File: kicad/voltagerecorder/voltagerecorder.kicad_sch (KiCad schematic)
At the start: 35 parts, among them J1 Conn_02x10_Odd_Even, J2 Phoenix Stecker, J3 Conn_01x08, J8 Conn_01x02, U1 Opamp_Quad, U5 ADS8638, U6 ESP32-S3-WROOM-2, Y1 32.768kHz

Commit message: sd card hinzugefügt
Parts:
- removed Y1: 32.768kHz, Crystal:Crystal_SMD_SeikoEpson_MC306-4Pin_8.0x3.2mm_HandSoldering, symbol Device:Crystal
- added J9: Micro_SD_Card, Connector_Card:microSD_HC_Hirose_DM3BT-DSF-PEJS, symbol Connector:Micro_SD_Card
- added Y1: Crystal_GND23, Crystal:Crystal_SMD_SeikoEpson_MC306-4Pin_8.0x3.2mm_HandSoldering, symbol Device:Crystal_GND23
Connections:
- net at C24.1, U6.8 (GPIO15/U0RTS/ADC2_CH4/XTAL_32K_P): now also Y1.4
- net at C29.1, U6.9 (GPIO16/U0CTS/ADC2_CH5/XTAL_32K_NH5): now also Y1.1
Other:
- note added: "2 pin Pheonix Trigger in and out"
- note added: "3 pin 5V, 24V, GND"
- note added: "AC/DC 230V 5V ??"
- note added: "DC/DC 24V 5V ??"
- note added: "SD Karte"
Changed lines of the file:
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@@
   (junction (at 160.02 81.28) (diameter 0) (color 0 0 0 0)
   )
-  (junction (at 110.49 194.31) (diameter 0) (color 0 0 0 0)
-  )
   (junction (at 171.45 73.66) (diameter 0) (color 0 0 0 0)
   )
@@
   (junction (at 110.49 142.24) (diameter 0) (color 0 0 0 0)
   )
-  (junction (at 110.49 201.93) (diameter 0) (color 0 0 0 0)
+  (junction (at 111.76 194.31) (diameter 0) (color 0 0 0 0)
   )
   (junction (at 270.51 58.42) (diameter 0) (color 0 0 0 0)
@@
   (junction (at 160.02 99.06) (diameter 0) (color 0 0 0 0)
   )
+  (junction (at 111.76 201.93) (diameter 0) (color 0 0 0 0)
+  )
   (junction (at 171.45 81.28) (diameter 0) (color 0 0 0 0)
   )
@@
     (stroke (width 0) (type default) (color 0 0 0 0))
   )
-  (wire (pts (xy 125.73 194.31) (xy 110.49 194.31))
+  (wire (pts (xy 106.68 194.31) (xy 111.76 194.31))
     (stroke (width 0) (type default) (color 0 0 0 0))
   )
@@
     (stroke (width 0) (type default) (color 0 0 0 0))
   )
-  (wire (pts (xy 106.68 194.31) (xy 110.49 194.31))
-    (stroke (width 0) (type default) (color 0 0 0 0))
-  )
   (wire (pts (xy 297.18 66.04) (xy 297.18 68.58))
     (stroke (width 0) (type default) (color 0 0 0 0))
@@
     (stroke (width 0) (type default) (color 0 0 0 0))
   )
+  (wire (pts (xy 111.76 194.31) (xy 125.73 194.31))
+    (stroke (width 0) (type default) (color 0 0 0 0))
+  )
   (wire (pts (xy 297.18 48.26) (xy 297.18 50.8))
     (stroke (width 0) (type default) (color 0 0 0 0))
@@
     (stroke (width 0) (type default) (color 0 0 0 0))
   )
+  (wire (pts (xy 111.76 201.93) (xy 125.73 201.93))
+    (stroke (width 0) (type default) (color 0 0 0 0))
+  )
   (wire (pts (xy 171.45 86.36) (xy 179.07 86.36))
     (stroke (width 0) (type default) (color 0 0 0 0))
@@
     (stroke (width 0) (type default) (color 0 0 0 0))
   )
-  (wire (pts (xy 106.68 201.93) (xy 110.49 201.93))
-    (stroke (width 0) (type default) (color 0 0 0 0))
-  )
   (wire (pts (xy 130.81 106.68) (xy 134.62 106.68))
     (stroke (width 0) (type default) (color 0 0 0 0))
@@
     (stroke (width 0) (type default) (color 0 0 0 0))
   )
-  (wire (pts (xy 125.73 201.93) (xy 110.49 201.93))
+  (wire (pts (xy 106.68 201.93) (xy 111.76 201.93))
     (stroke (width 0) (type default) (color 0 0 0 0))
   )
@@
   (wire (pts (xy 74.93 71.12) (xy 74.93 64.77))
     (stroke (width 0) (type default) (color 0 0 0 0))
+  )
+  (text "AC/DC 230V 5V ??" (at 312.42 194.31 0)
+    (effects (font (size 2.54 2.54)) (justify left bottom))
   )
   (text "L1" (at 30.48 72.0725 0)
@@
     (effects (font (size 2.54 2.54)) (justify left bottom))
   )
+  (text "2 pin Pheonix Trigger in and out" (at 312.42 175.26 0)
+    (effects (font (size 2.54 2.54)) (justify left bottom))
+  )
   (text "AL_PD:\nlow active\ninternal pull up" (at 201.93 72.39 0)
     (effects (font (size 1.27 1.27)) (justify left bottom))
@@
   (text "L3" (at 30.48 77.1525 0)
     (effects (font (size 1.27 1.27)) (justify left bottom))
+  )
+  (text "DC/DC 24V 5V ??" (at 312.42 187.96 0)
+    (effects (font (size 2.54 2.54)) (justify left bottom))
+  )
+  (text "SD Karte" (at 312.42 168.91 0)
+    (effects (font (size 2.54 2.54)) (justify left bottom))
   )
   (text "C0G" (at 114.3 93.9801 0)
@@
     (at 129.54 115.57 0)
     (effects (font (size 1.27 1.27)) (justify left bottom))
+  )
+  (text "3 pin 5V, 24V, GND" (at 312.42 181.61 0)
+    (effects (font (size 2.54 2.54)) (justify left bottom))
   )
   (label "IN5_EXT" (at 87.63 41.91 270)
@@
     (pin "4")
   )
+  (symbol (lib_id "Connector:Micro_SD_Card") (at 325.12 224.79 0) (unit 1)
+    (in_bom yes) (on_board yes) (fields_autoplaced)
+    (property "Reference" "J9" (id 0) (at 325.755 205.74 0))
+    (property "Value" "Micro_SD_Card" (id 1) (at 325.755 208.28 0))
+    (property "Footprint" "Connector_Card:microSD_HC_Hirose_DM3BT-DSF-PEJS" (id 2) (at 354.33 217.17 0)
+      (effects (font (size 1.27 1.27)) hide)
+    )
+    (property "Datasheet" "http://katalog.we-online.de/em/datasheet/693072010801.pdf" (id 3) (at 325.12 224.79 0)
+      (effects (font (size 1.27 1.27)) hide)
+    )
+    (pin "1")
+    (pin "2")
+    (pin "3")
+    (pin "4")
+    (pin "5")
+    (pin "6")
+    (pin "7")
+    (pin "8")
+    (pin "9")
+  )
+  (symbol (lib_id "Device:Crystal_GND23") (at 111.76 198.12 90) (unit 1)
+    (in_bom yes) (on_board yes) (fields_autoplaced)
+    (property "Reference" "Y1" (id 0) (at 124.46 193.421 90))
+    (property "Value" "Crystal_GND23" (id 1) (at 124.46 195.961 90))
+    (property "Footprint" "Crystal:Crystal_SMD_SeikoEpson_MC306-4Pin_8.0x3.2mm_HandSoldering" (id 2) (at 111.76 198.12 0)
+      (effects (font (size 1.27 1.27)) hide)
+    )
+    (property "Datasheet" "~" (id 3) (at 111.76 198.12 0)
+      (effects (font (size 1.27 1.27)) hide)
+    )
+    (pin "1")
+    (pin "2")
+    (pin "3")
+    (pin "4")
+  )
   (symbol (lib_id "Device:C") (at 96.52 73.66 0) (unit 1)
     (in_bom yes) (on_board yes)
@@
     )
     (property "Datasheet" "~" (id 3) (at 171.45 90.17 0)
-      (effects (font (size 1.27 1.27)) hide)
-    )
-    (pin "1")
-    (pin "2")
-  )
-  (symbol (lib_id "Device:Crystal") (at 110.49 198.12 270) (unit 1)
-    (in_bom yes) (on_board yes) (fields_autoplaced)
-    (property "Reference" "Y1" (id 0) (at 114.3 196.8499 90)
-      (effects (font (size 1.27 1.27)) (justify left))
-    )
-    (property "Value" "32.768kHz" (id 1) (at 114.3 199.3899 90)
-      (effects (font (size 1.27 1.27)) (justify left))
-    )
-    (property "Footprint" "Crystal:Crystal_SMD_SeikoEpson_MC306-4Pin_8.0x3.2mm_HandSoldering" (id 2) (at 110.49 198.12 0)
-      (effects (font (size 1.27 1.27)) hide)
-    )
-    (property "Datasheet" "~" (id 3) (at 110.49 198.12 0)
       (effects (font (size 1.27 1.27)) hide)
     )
@@
       (reference "J8") (unit 1) (value "Conn_01x02") (footprint "Connector_PinHeader_2.54mm:PinHeader_1x02_P2.54mm_Vertical")
     )
+    (path "/9c543bc0-4531-49c8-a9a3-3bab9988c097"
+      (reference "J9") (unit 1) (value "Micro_SD_Card") (footprint "Connector_Card:microSD_HC_Hirose_DM3BT-DSF-PEJS")
+    )
     (path "/9767ed14-54f6-47aa-91eb-a27d04c45e2a"
       (reference "JP1") (unit 1) (value "SolderJumper_3_Open") (footprint "Jumper:SolderJumper-3_P1.3mm_Open_RoundedPad1.0x1.5mm")
@@
       (reference "U7") (unit 1) (value "L78L12ACUTR") (footprint "Package_TO_SOT_SMD:SOT-89-3_Handsoldering")
     )
-    (path "/bd8055c5-bb05-44e7-a2eb-64493be9f622"
-      (reference "Y1") (unit 1) (value "32.768kHz") (footprint "Crystal:Crystal_SMD_SeikoEpson_MC306-4Pin_8.0x3.2mm_HandSoldering")
-    )
-  )
+    (path "/a087b7ce-d9b0-4ba0-8285-fc2f36d419e2"
+      (reference "Y1") (unit 1) (value "Crystal_GND23") (footprint "Crystal:Crystal_SMD_SeikoEpson_MC306-4Pin_8.0x3.2mm_HandSoldering")
+    )
+  )

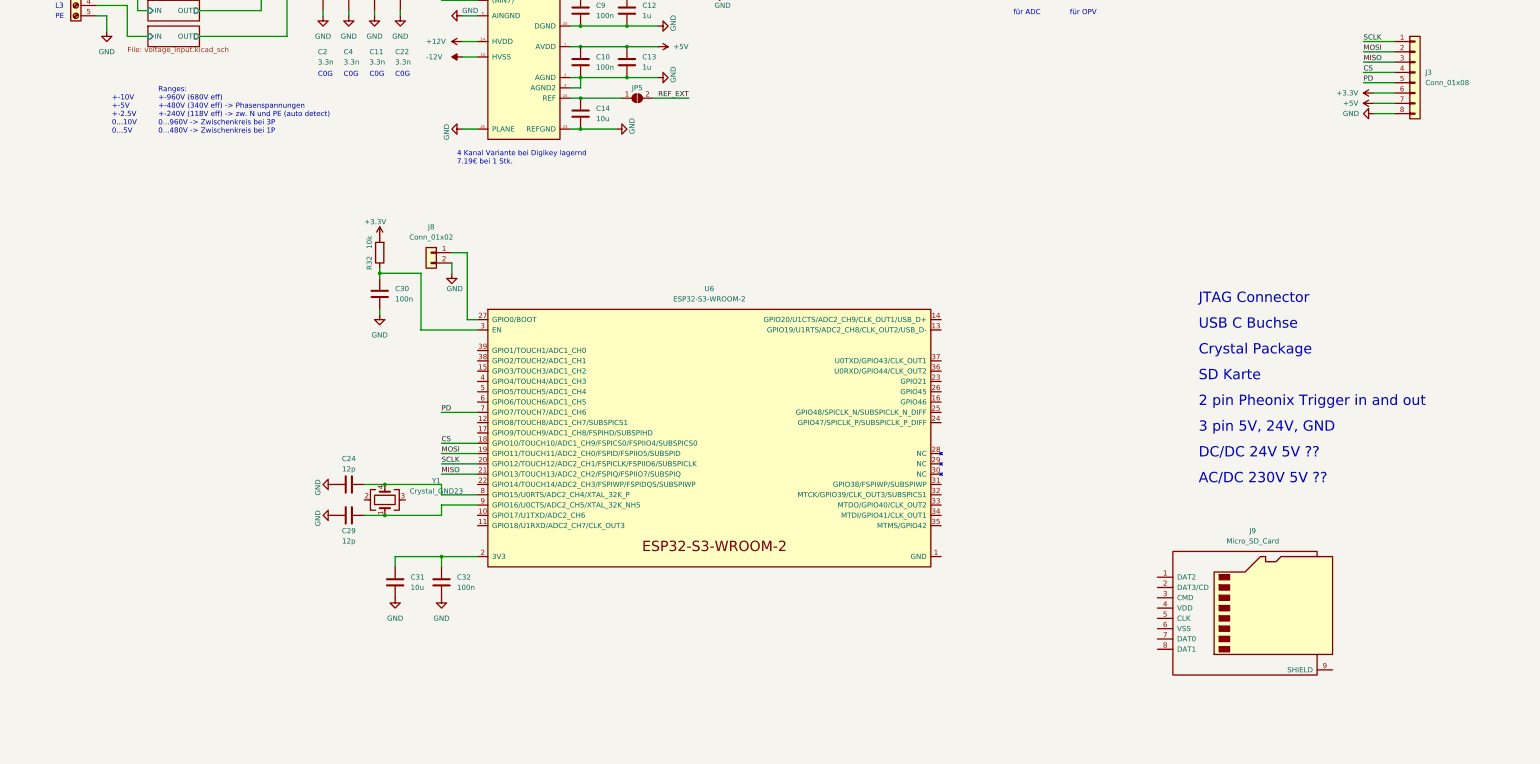
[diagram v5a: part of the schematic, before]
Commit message: SD und USB-C added.
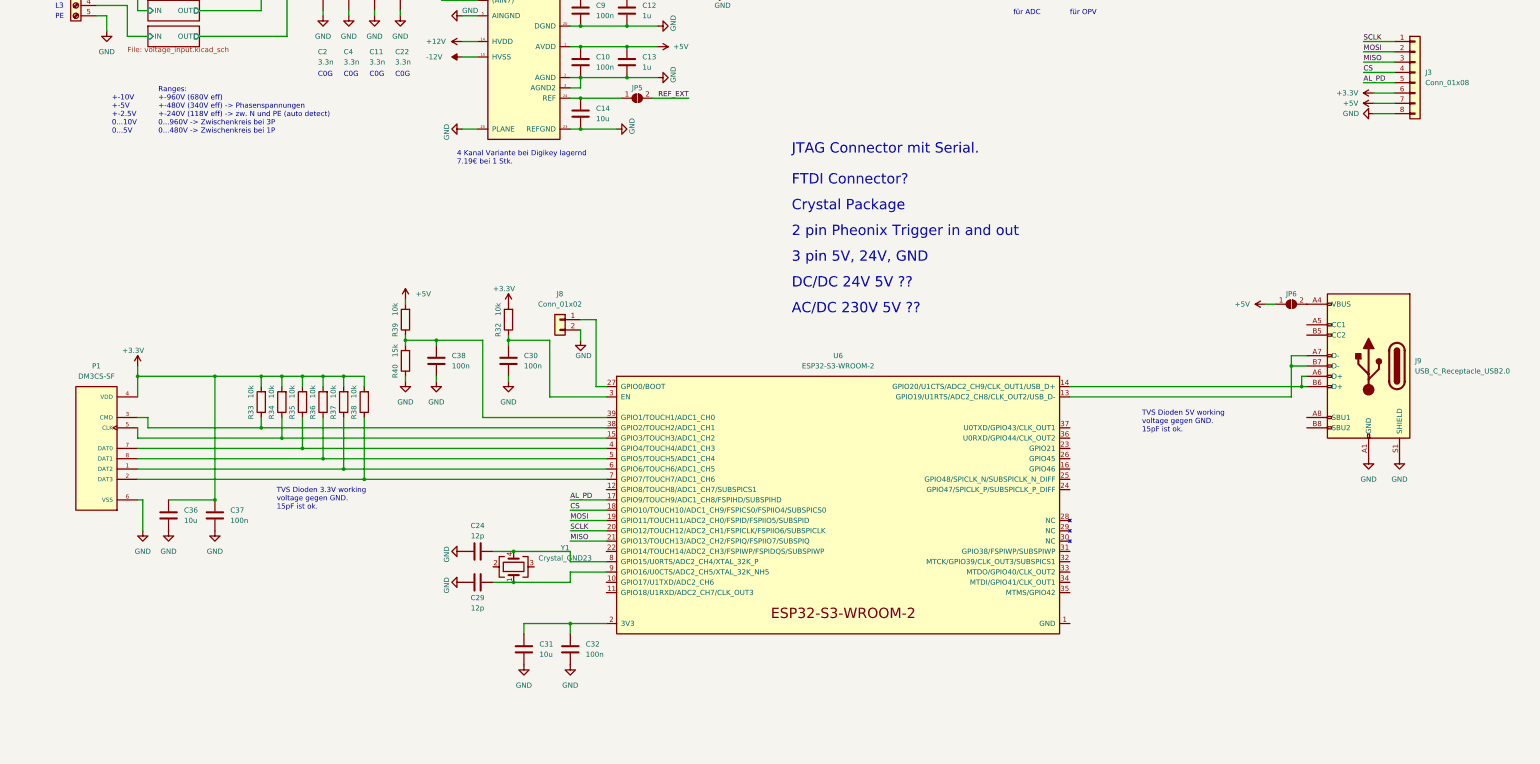
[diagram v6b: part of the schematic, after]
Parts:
- removed J9: Micro_SD_Card, Connector_Card:microSD_HC_Hirose_DM3BT-DSF-PEJS, symbol Connector:Micro_SD_Card
- added C36: 10u, Capacitor_SMD:C_0805_2012Metric_Pad1.18x1.45mm_HandSolder, symbol Device:C
- added C37, C38: 100n, Capacitor_SMD:C_0603_1608Metric_Pad1.08x0.95mm_HandSolder, symbol Device:C
- added J9: USB_C_Receptacle_USB2.0, Connector_USB:USB_C_Receptacle_GCT_USB4085, symbol Connector:USB_C_Receptacle_USB2.0
- added JP6: SolderJumper_2_Open, Jumper:SolderJumper-2_P1.3mm_Open_RoundedPad1.0x1.5mm, symbol Jumper:SolderJumper_2_Open
- added P1: DM3CS-SF, Hirose:HRS_DM3CS-SF, symbol Hirose:DM3CS-SF
- added R33, R34, R35, R36, R37, R38, R39: 10k, Resistor_SMD:R_0603_1608Metric_Pad0.98x0.95mm_HandSolder, symbol Device:R
- added R40: 15k, Resistor_SMD:R_0603_1608Metric_Pad0.98x0.95mm_HandSolder, symbol Device:R
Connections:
- net +3.3V: now also C36.1, C37.1, P1.4 (VDD), R33.2, R34.2, R35.2, R36.2, R37.2, R38.2
- net +5V: now also JP6.1 (A), R39.2
- net AL_PD: now also J3.5 (Pin_5), U6.17 (GPIO9/TOUCH9/ADC1_CH8/FSPIHD/SUBSPIHD)
- net GND: now also C36.2, C37.2, C38.2, J9.A1 (GND), J9.A12 (GND), J9.B1 (GND), J9.B12 (GND), J9.S1 (SHIELD), P1.6 (VSS), R40.1
- net at U6.13 (GPIO19/U1RTS/ADC2_CH8/CLK_OUT2/USB_D-): now also J9.A7 (D-), J9.B7 (D-)
- net at U6.14 (GPIO20/U1CTS/ADC2_CH9/CLK_OUT1/USB_D+): now also J9.A6 (D+), J9.B6 (D+)
- net at U6.15 (GPIO3/TOUCH3/ADC1_CH2): now also P1.5 (CLK), R34.1
- net at U6.38 (GPIO2/TOUCH2/ADC1_CH1): now also P1.3 (CMD), R33.1
- net at U6.39 (GPIO1/TOUCH1/ADC1_CH0): now also C38.1, R39.1, R40.2
- net at U6.4 (GPIO4/TOUCH4/ADC1_CH3): now also P1.7 (DAT0), R35.1
- net at U6.5 (GPIO5/TOUCH5/ADC1_CH4): now also P1.8 (DAT1), R36.1
- net at U6.6 (GPIO6/TOUCH6/ADC1_CH5): now also P1.1 (DAT2), R37.1
- net PD: no longer names the net of U6.7 (GPIO7/TOUCH7/ADC1_CH6)
- net PD: now also P1.2 (DAT3), R38.1; no longer J3.5 (Pin_5)
- new net: J9.A4 (VBUS), J9.A9 (VBUS), J9.B4 (VBUS), J9.B9 (VBUS), JP6.2 (B)
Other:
- note added: "FTDI Connector?"
- note added: "JTAG Connector mit Serial."
- note added: "TVS Dioden 3.3V working voltage gegen GND. 15pF ist ok."
- note added: "TVS Dioden 5V working voltage gegen GND. 15pF ist ok."
- note removed: "JTAG Connector"
- note removed: "SD Karte"
- note removed: "USB C Buchse"
- moved on the sheet: C24, C29, C30, C31, C32, J8, R32, U6, Y1

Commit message: a
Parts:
- removed C24, C29: 12p, Capacitor_SMD:C_0603_1608Metric_Pad1.08x0.95mm_HandSolder, symbol Device:C
- removed C30, C32: 100n, Capacitor_SMD:C_0603_1608Metric_Pad1.08x0.95mm_HandSolder, symbol Device:C
- removed C31: 10u, Capacitor_SMD:C_0805_2012Metric_Pad1.18x1.45mm_HandSolder, symbol Device:C
- removed J2: Phoenix Stecker, Connector_Phoenix_MC_HighVoltage:PhoenixContact_MC_1,5_5-G-5.08_1x05_P5.08mm_Horizontal, symbol Connector:Screw_Terminal_01x05
- removed J8: Conn_01x02, Connector_PinHeader_2.54mm:PinHeader_1x02_P2.54mm_Vertical, symbol Connector_Generic:Conn_01x02
- removed J9: USB_C_Receptacle_USB2.0, Connector_USB:USB_C_Receptacle_GCT_USB4085, symbol Connector:USB_C_Receptacle_USB2.0
- removed JP6: SolderJumper_2_Open, Jumper:SolderJumper-2_P1.3mm_Open_RoundedPad1.0x1.5mm, symbol Jumper:SolderJumper_2_Open
- removed R32: 10k, Resistor_SMD:R_0603_1608Metric_Pad0.98x0.95mm_HandSolder, symbol Device:R
- removed U6: ESP32-S3-WROOM-2, Espressif:ESP32-S3-WROOM-2, symbol espressif:ESP32-S3-WROOM-2
- removed Y1: Crystal_GND23, Crystal:Crystal_SMD_SeikoEpson_MC306-4Pin_8.0x3.2mm_HandSoldering, symbol Device:Crystal_GND23
- added C? (x6): 100nF, Capacitor_SMD:C_0603_1608Metric, symbol Device:C
- added C? (x2): 10nF, Capacitor_SMD:C_0603_1608Metric, symbol Device:C
- added C? (x2): 1uF, Capacitor_SMD:C_0603_1608Metric, symbol Device:C
- added C?: 1u, Capacitor_SMD:C_0603_1608Metric_Pad1.08x0.95mm_HandSolder, symbol Device:C
- added C? (x2): 22pF, Capacitor_SMD:C_0603_1608Metric, symbol Device:C
- added C?: 4.7uF, Capacitor_SMD:C_0603_1608Metric, symbol Device:C
- added D?: D_Schottky, Diode_SMD:D_0603_1608Metric_Pad1.05x0.95mm_HandSolder, symbol Device:D_Schottky
- added D?: RED, Diode_SMD:D_0603_1608Metric, symbol Device:LED_Filled
- added D?: GREEN, Diode_SMD:D_0603_1608Metric, symbol Device:LED_Filled
- added D?: YELLOW, Diode_SMD:D_0603_1608Metric, symbol Device:LED_Filled
- added FB?: 220R / 100MHz, Inductor_SMD:L_0603_1608Metric_Pad1.05x0.95mm_HandSolder, symbol Device:FerriteBead
- added H? (x6): MountingHole_Pad, MountingHole:MountingHole_3.2mm_M3_DIN965_Pad, symbol Mechanical:MountingHole_Pad
- added J?: Conn_01x05, Connector_Phoenix_MSTB:PhoenixContact_MSTBA_2,5_5-G-5,08_1x05_P5.08mm_Horizontal, symbol Connector_Generic:Conn_01x05
- added J? (x2): Conn_01x02, Connector_PinHeader_2.54mm:PinHeader_1x02_P2.54mm_Vertical, symbol Connector_Generic:Conn_01x02
- added J? (x2): USB_C_Receptacle_USB2.0, Connector_USB:USB_C_Receptacle_XKB_U262-16XN-4BVC11, symbol Connector:USB_C_Receptacle_USB2.0
- added J?: Conn_01x08, Connector_PinHeader_2.54mm:PinHeader_1x08_P2.54mm_Horizontal, symbol Connector_Generic:Conn_01x08
- added R? (x2): 1M, Resistor_SMD:R_0603_1608Metric, symbol Device:R
- added R? (x3): 1k, Resistor_SMD:R_0603_1608Metric, symbol Device:R
- added R?: 10k, Resistor_SMD:R_0603_1608Metric, symbol Device:R
- added R?: 100k, Resistor_SMD:R_0603_1608Metric, symbol Device:R
- added R? (x2): 3k3, Resistor_SMD:R_0603_1608Metric_Pad0.98x0.95mm_HandSolder, symbol Device:R
- added U8: ESP32-C3-WROOM-02, Espressif:ESP32-C3-WROOM-02, symbol espressif:ESP32-C3-WROOM-02
- added U?: ESP-PSRAM32, Package_SO:SOIC-8_3.9x4.9mm_P1.27mm, symbol Memory_RAM:ESP-PSRAM32
- added U? (x2): STM32G473CBT6, Package_QFP:LQFP-48_7x7mm_P0.5mm, symbol wittmann:STM32G473CBT6
- added Y?: 24MHz, Crystal:Crystal_SMD_3225-4Pin_3.2x2.5mm, symbol Device:Crystal_GND24
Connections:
- net +3.3V: now also C?.1, D?.2 (A), D?.2 (A), D?.2 (A), R?.2, R?.2, U?.8 (VCC)
- net +5V: now also D?.2 (A)
- net GND: now also C?.2, C?.2, C?.2, C?.2, C?.2, C?.2, C?.2, C?.2, C?.2, C?.2, C?.2, C?.2, C?.2, C?.2, J?.1 (Pin_1), J?.2 (Pin_2), J?.5 (Pin_5), J?.7 (Pin_7), J?.A1 (GND), J?.A1 (GND), J?.A12 (GND), J?.A12 (GND), J?.B1 (GND), J?.B1 (GND), J?.B12 (GND), J?.B12 (GND), R?.1, R?.2, R?.2, U8.19 (GND), U8.9 (GND), U?.19 (VSSA), U?.23 (VSS), U?.35 (VSS), U?.4 (VSS), U?.47 (VSS), Y?.2, Y?.4
- net voltage_input/IN: now also J?.2 (Pin_2)
- net voltage_input1/IN: now also J?.3 (Pin_3)
- net voltage_input2/IN: now also J?.4 (Pin_4)
- net voltage_input3/IN: now also J?.1 (Pin_1)
- new net: D?.1 (K), J?.A4 (VBUS), J?.A4 (VBUS), J?.A9 (VBUS), J?.A9 (VBUS), J?.B4 (VBUS), J?.B4 (VBUS), J?.B9 (VBUS), J?.B9 (VBUS)
- new net: D?.1 (K), R?.1 (x3)
- new net: C?.1, U?.5 (PF0-OSC_IN), Y?.1
- new net: C?.1, U?.6 (PF1-OSC_OUT), Y?.3
- new net 3V3: C?.1, C?.1, C?.1, C?.1, FB?.1, J?.2 (Pin_2), R?.2, U?.1 (VBAT), U?.24 (VDD), U?.36 (VDD), U?.48 (VDD)
- new net 3V3-EN: U?.2 (PC13)
- new net 3V3-FAULT: U?.4 (PC15-OSC32_OUT)
- new net 5V-FAULT: U?.3 (PC14-OSC32_IN)
- new net BOOT0: J?.1 (Pin_1), R?.2, U?.45 (PB8-BOOT0)
- new net LED-GREEN: R?.2, U?.16 (PB0)
- new net LED-RED: R?.2, U?.18 (PB2)
- new net LED-YELLOW: R?.2, U?.17 (PB1)
- new net NRST: C?.1, J?.8 (Pin_8), R?.1, U?.7 (PG10-NRST)
- new net RAM_CLK: U?.6 (SCLK)
- new net RAM_CS: U?.1 (~{CE})
- new net RAM_SIO0: U?.2 (SO/SIO)
- new net RAM_SIO1: U?.5 (SI/SIO)
- new net RAM_SIO2: U?.3 (SIO2)
- new net RAM_SIO3: U?.7 (SIO3)
- new net SHIELD: C?.1, C?.1, H?.1, H?.1, H?.1, H?.1, H?.1, H?.1, J?.S1 (SHIELD), J?.S1 (SHIELD), R?.1, R?.1
- new net SWDCLK: J?.4 (Pin_4), U?.38 (PA14)
- new net SWDIO: J?.3 (Pin_3), U?.37 (PA13)
- new net TRACE-IN: J?.6 (Pin_6), U?.32 (PA10)
- new net TRACE-OUT: J?.5 (Pin_5), U?.31 (PA9)
- new net USB-D+: J?.A6 (D+), J?.A6 (D+), J?.B6 (D+), J?.B6 (D+), U?.34 (PA12)
- new net USB-D-: J?.A7 (D-), J?.A7 (D-), J?.B7 (D-), J?.B7 (D-), U?.33 (PA11)
- new net USB_CC1: J?.1 (Pin_1), J?.A5 (CC1), J?.A5 (CC1), R?.1, U?.41 (PB4), U?.42 (PB5)
- new net USB_CC2: J?.2 (Pin_2), J?.B5 (CC2), J?.B5 (CC2), R?.1, U?.43 (PB6), U?.44 (PB7)
- new net VDDA: C?.1, C?.1, FB?.2, U?.21 (VDDA)
- new net VREF+: C?.1, C?.1, U?.20 (VREF+)
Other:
- note added: "N"
- note added: "OSC-OUT"
- note added: "PA10"
- note added: "PA9"
- note added: "PB4"
- note added: "PB6"
- note added: "SPI?"
- note added: "Trigger in and out"
- note removed: "2 pin Pheonix Trigger in and out"
- note removed: "3 pin 5V, 24V, GND"
- note removed: "AC/DC 230V 5V ??"
- note removed: "Crystal Package"
- note removed: "DC/DC 24V 5V ??"
- note removed: "FTDI Connector?"
- note removed: "JTAG Connector mit Serial."
- note removed: "TVS Dioden 5V working voltage gegen GND. 15pF ist ok."
- moved on the sheet: C1, C10, C11, C12, C13, C14, C2, C22, C26, C28, C3, C36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
